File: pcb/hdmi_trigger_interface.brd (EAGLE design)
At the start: 78.7 x 63.5 mm, 60 parts, among them U1 TPD12S016PWR, U2 TPD12S016PWR, X1 87438-06, X2 87438-06, Y1 SI514

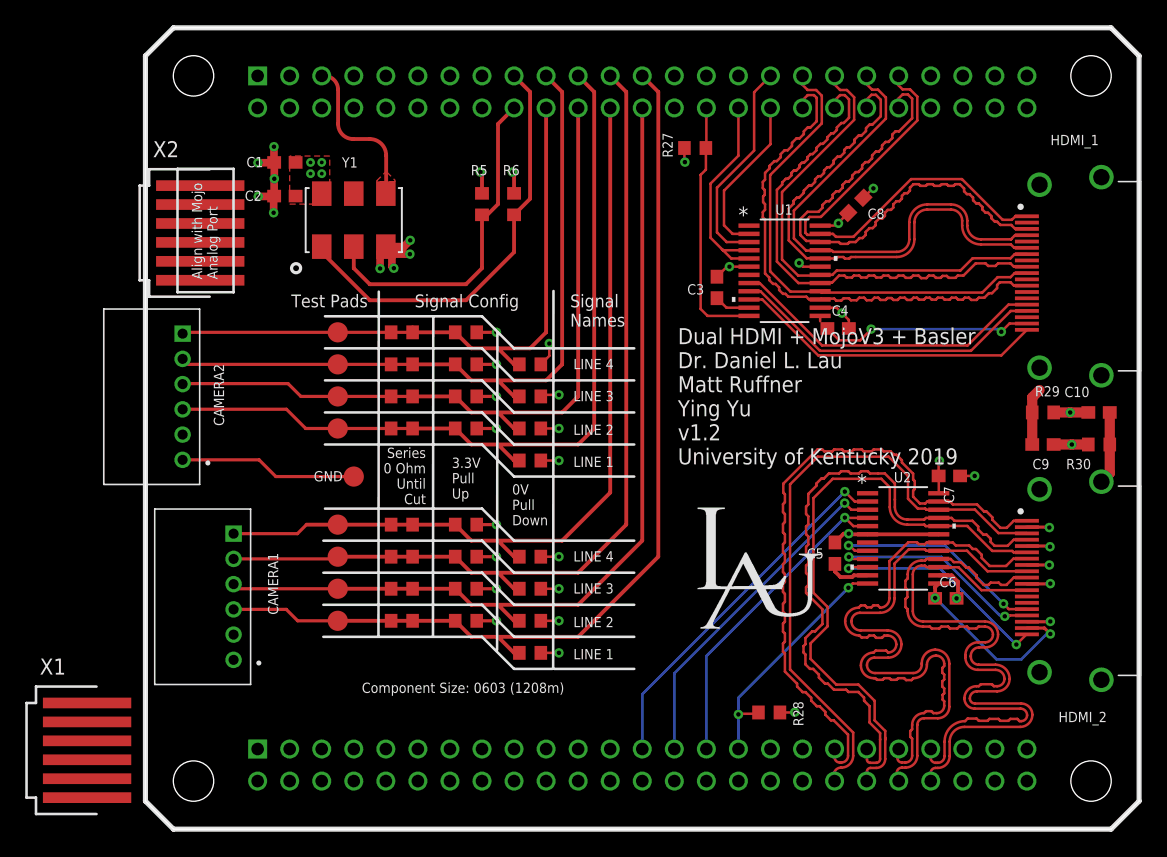
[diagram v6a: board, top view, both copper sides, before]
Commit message: finished routing with new spacing and layout.
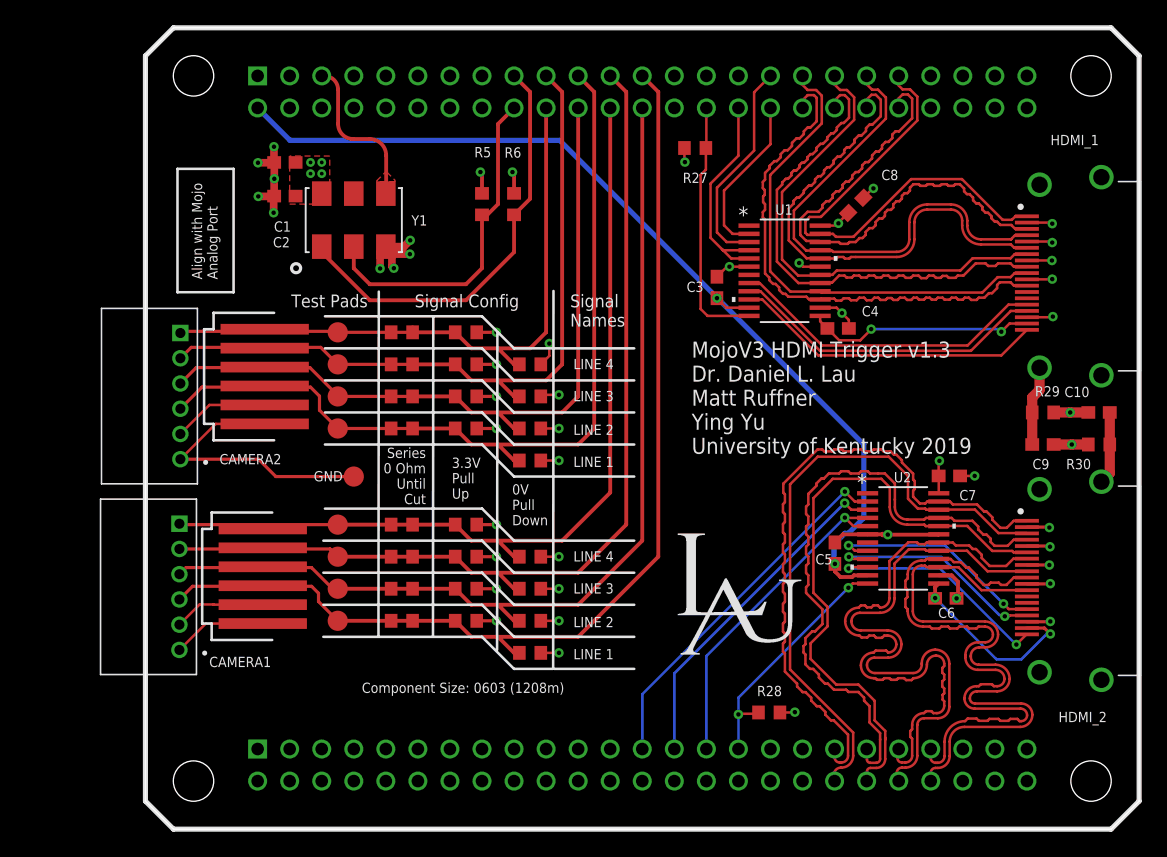
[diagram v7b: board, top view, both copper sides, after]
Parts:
- moved X1 19.6 mm to (9.30, 20.0)
- moved X2 12.5 mm to (9.45, 35.9)
- moved CAMERA1 4.36 mm to (2.69, 19.2)
- moved CAMERA2 0.18 mm to (2.77, 34.3)
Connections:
- net GND: now also X1.5, X1.6, X2.5, X2.6
- net N$10: now also X2.2
- net N$11: now also X2.3
- net N$12: now also X2.4
- net N$5: now also X1.1
- net N$6: now also X1.2
- net N$7: now also X1.3
- net N$8: now also X1.4
- net N$9: now also X2.1
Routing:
- net 5V: track 6.28 -> 76.1 mm, vias 0 -> 2
- net GND: track 79.1 -> 119.7 mm, vias 31 -> 36
- net N$8: track 12.9 -> 18.7 mm
- net N$7: track 12.6 -> 17.7 mm
- net N$6: track 13.0 -> 17.4 mm
- net N$5: track 12.8 -> 16.8 mm
- net N$12: track 18.6 -> 20.9 mm
- net N$13: track 4.55 -> 6.33 mm
- net N$11: track 18.4 -> 19.7 mm
- net N$10: track 18.6 -> 19.5 mm
- net 5VHDMI1: track 17.5 -> 18.3 mm
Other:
- board text added: "MojoV3 HDMI Trigger v1.3 Dr. Daniel L. Lau Matt Ruffner Ying Yu University of Kentucky 2019"
- board text removed: "Dual HDMI + MojoV3 + Basler Dr. Daniel L. Lau Matt Ruffner Ying Yu v1.2 University of Kentucky 2019"
